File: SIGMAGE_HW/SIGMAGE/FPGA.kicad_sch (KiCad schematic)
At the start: 1 part, among them U8 LFE5U25F6BG256I

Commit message: some FPGA stuff
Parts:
- added C100, C101, C103, C104, C106, C107, C109, C110, C49, C51, C52, C53, C54, C55, C91, C92, C94, C95, C97, C98: 100n, Capacitor_SMD:C_0603_1608Metric, symbol Device:C
- added C102, C105, C108, C111, C50, C93, C96, C99: 10u, Capacitor_SMD:C_0603_1608Metric, symbol Device:C
- added R48, R49, R50, R51, R52, R53, R54, R55: 0, Resistor_SMD:R_0603_1608Metric, symbol Device:R
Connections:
- net GND: now also C100.2, C101.2, C102.2, C103.2, C104.2, C105.2, C106.2, C107.2, C108.2, C109.2, C110.2, C111.2, C49.2, C50.2, C51.2, C52.2, C53.2, C54.2, C55.2, C91.2, C92.2, C93.2, C94.2, C95.2, C96.2, C97.2, C98.2, C99.2
- net VCC_CORE: now also C49.1, C50.1, C51.1, C52.1, C53.1, C54.1, C55.1, R48.2
- net VCC_IO1: now reaches U8.F10 (VCCIO1_1)
- net VCC_IO1: now also U8.F11 (VCCIO1_2), C94.1, C95.1, C96.1, R50.2
- net VCC_IO0: now reaches U8.F6 (VCCIO0_1)
- net VCC_IO0: now also U8.F7 (VCCIO0_2), C91.1, C92.1, C93.1, R49.2
- net VCC_IO2: now reaches U8.H11 (VCCIO2_1)
- net VCC_IO2: now also U8.J11 (VCCIO2_2), C97.1, C98.1, C99.1, R51.2
- net VCC_IO7: now reaches U8.H6 (VCCIO7_1)
- net VCC_IO7: now also U8.H7 (VCCIO7_2), C106.1, C107.1, C108.1, R54.2
- net VCC_IO6: now reaches U8.J6 (VCCIO6_1)
- net VCC_IO6: now also U8.J7 (VCCIO6_2), C103.1, C104.1, C105.1, R53.2
- net VCC_IO3: now reaches U8.K11 (VCCIO3_1)
- net VCC_IO3: now also U8.L11 (VCCIO3_2), C100.1, C101.1, C102.1, R52.2
- net VCC_IO8: now reaches U8.L6 (VCCIO8)
- net VCC_IO8: now also C109.1, C110.1, C111.1, R55.2
- net FPGA_JTAG_TDO: now reaches U8.M10 (TDO)
- net FPGA_JTAG_TDI: now reaches U8.R11 (TDI)
- net FPGA_JTAG_TCK: now reaches U8.T10 (TCK)
- net FPGA_JTAG_TMS: now reaches U8.T11 (TMS)
- new net DVCC_1V2: R48.1
- new net DVCC_3V3: R49.1, R50.1, R51.1, R52.1, R53.1, R54.1, R55.1
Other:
- moved on the sheet: U8A, U8B, U8C, U8D, U8E, U8F, U8G, U8H, U8I

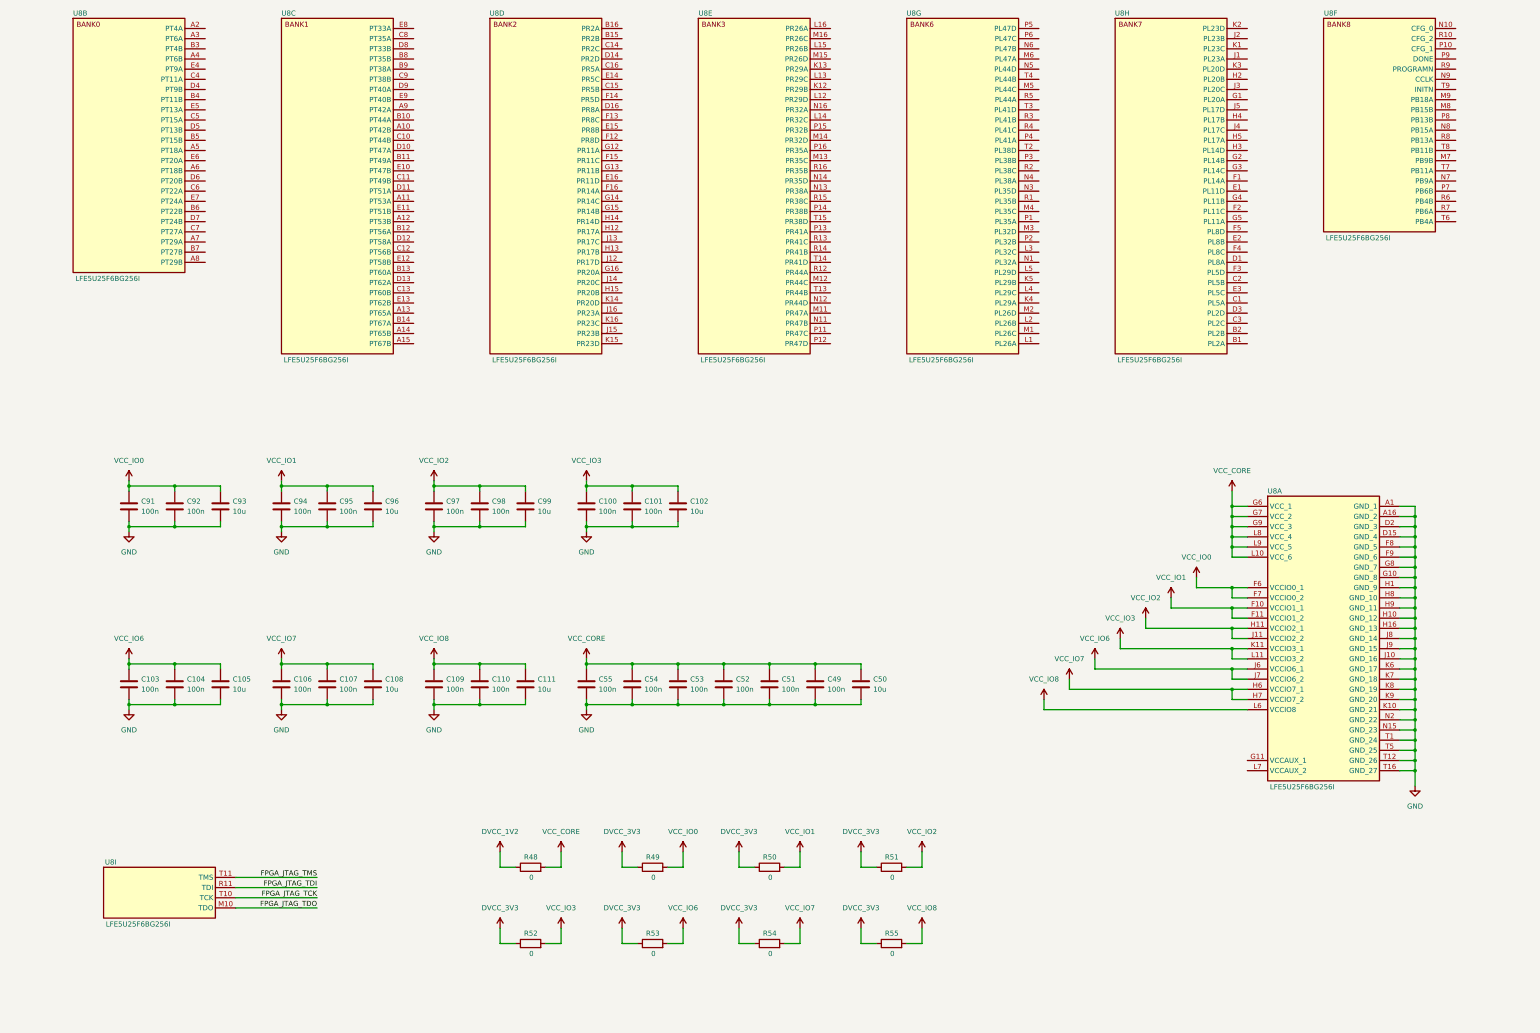
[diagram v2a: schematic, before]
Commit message: added SPI flash
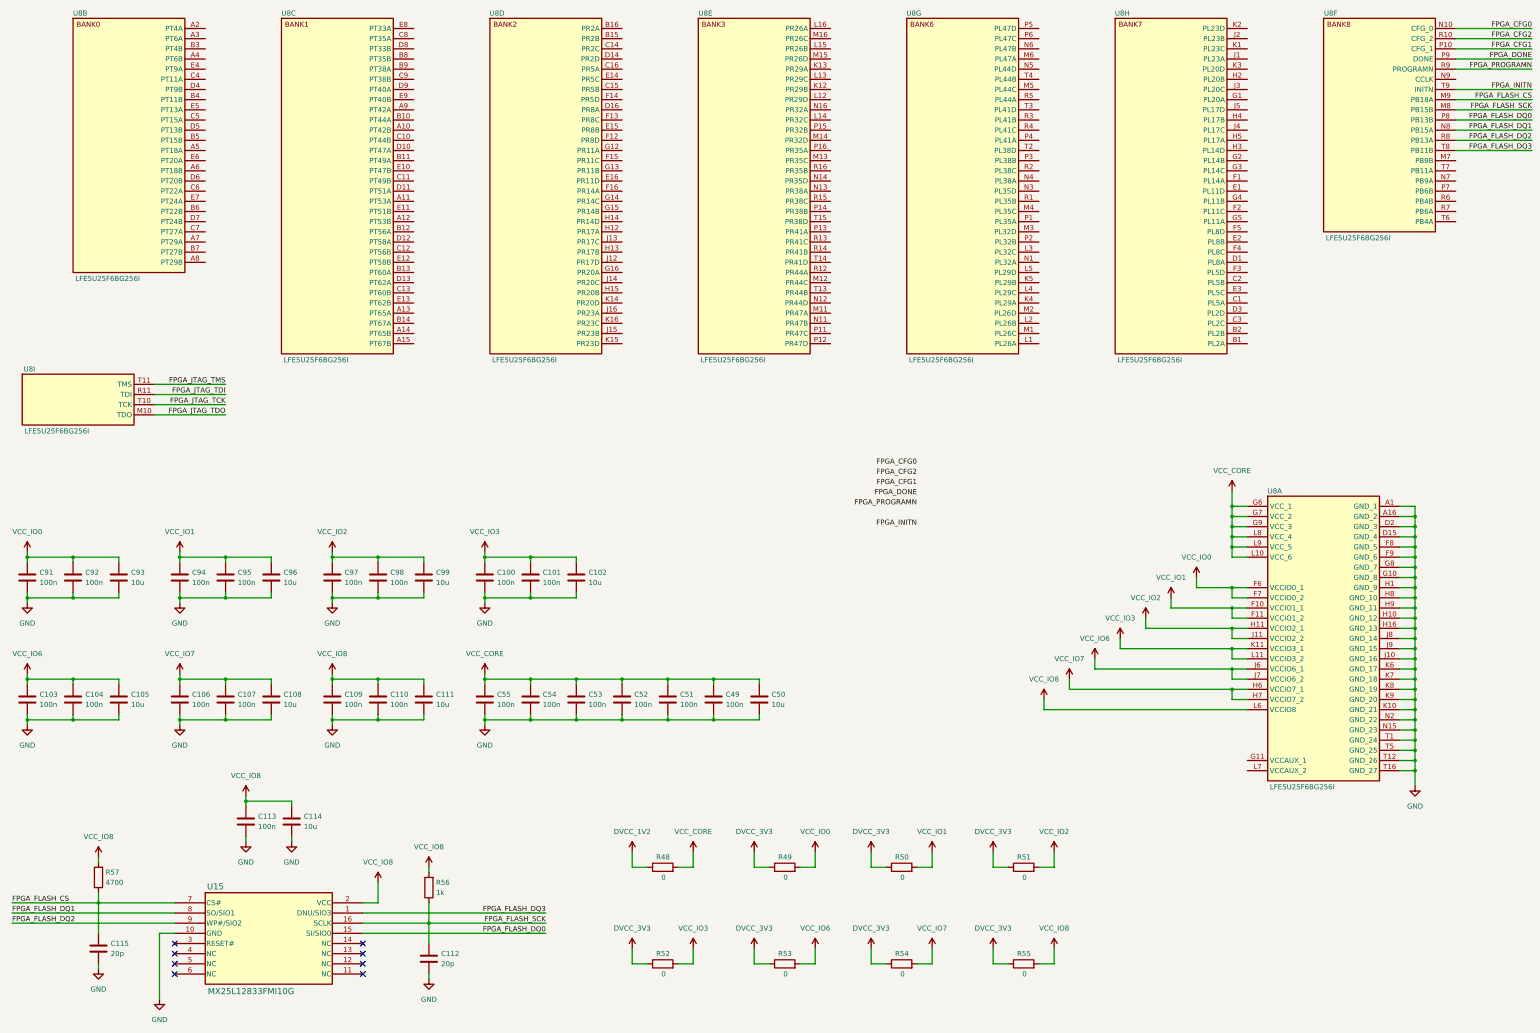
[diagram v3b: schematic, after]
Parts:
- added C112, C115: 20p, Capacitor_SMD:C_0603_1608Metric, symbol Device:C
- added C113: 100n, Capacitor_SMD:C_0603_1608Metric, symbol Device:C
- added C114: 10u, Capacitor_SMD:C_0603_1608Metric, symbol Device:C
- added R56: 1k, Resistor_SMD:R_0603_1608Metric, symbol Device:R
- added R57: 4700, Resistor_SMD:R_0603_1608Metric, symbol Device:R
- added U15: MX25L12833FMI10G, SIGMAGE:MX25L12833FMI10G, symbol SIGMAGE:MX25L12833FMI10G
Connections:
- net GND: now also C112.2, C113.2, C114.2, C115.2, U15.10 (GND)
- net VCC_IO8: now also C113.1, C114.1, R56.2, R57.2, U15.2 (VCC)
- net FPGA_FLASH_SCK: now reaches U8.M8 (PB15B)
- net FPGA_FLASH_SCK: now also C112.1, R56.1, U15.16 (SCLK)
- net FPGA_FLASH_CS: now reaches U8.M9 (PB18A)
- net FPGA_FLASH_CS: now also C115.1, R57.1, U15.7 (CS#)
- net FPGA_CFG0: now reaches U8.N10 (CFG_0)
- net FPGA_FLASH_DQ1: now reaches U8.N8 (PB15A)
- net FPGA_FLASH_DQ1: now also U15.8 (SO/SIO1)
- net FPGA_CFG1: now reaches U8.P10 (CFG_1)
- net FPGA_FLASH_DQ0: now reaches U8.P8 (PB13B)
- net FPGA_FLASH_DQ0: now also U15.15 (SI/SIO0)
- net FPGA_DONE: now reaches U8.P9 (DONE)
- net FPGA_CFG2: now reaches U8.R10 (CFG_2)
- net FPGA_FLASH_DQ2: now reaches U8.R8 (PB13A)
- net FPGA_FLASH_DQ2: now also U15.9 (WP#/SIO2)
- net FPGA_PROGRAMN: now reaches U8.R9 (PROGRAMN)
- net FPGA_FLASH_DQ3: now reaches U8.T8 (PB11B)
- net FPGA_FLASH_DQ3: now also U15.1 (DNU/SIO3)
- net FPGA_INITN: now reaches U8.T9 (INITN)
- no-connect marks 0 -> 8
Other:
- moved on the sheet: C100, C101, C102, C103, C104, C105, C106, C107, C108, C109, C110, C111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

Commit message: some changes
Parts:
- removed C112, C115: 20p, Capacitor_SMD:C_0603_1608Metric, symbol Device:C
- removed C113: 100n, Capacitor_SMD:C_0603_1608Metric, symbol Device:C
- removed C114: 10u, Capacitor_SMD:C_0603_1608Metric, symbol Device:C
- removed R56: 1k, Resistor_SMD:R_0603_1608Metric, symbol Device:R
- removed R57: 4700, Resistor_SMD:R_0603_1608Metric, symbol Device:R
- removed U15: MX25L12833FMI10G, SIGMAGE:MX25L12833FMI10G, symbol SIGMAGE:MX25L12833FMI10G
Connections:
- no-connect marks 8 -> 0

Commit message: changes
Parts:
- removed R48, R49, R50, R51, R52, R53, R54, R55: 0, Resistor_SMD:R_0603_1608Metric, symbol Device:R
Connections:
- net VCC_CORE is gone; now on net DVCC_1V2: C49.1, C50.1, C51.1, C52.1, C53.1, C54.1, C55.1, U8.G6 (VCC_1), U8.G7 (VCC_2), U8.G9 (VCC_3), U8.L10 (VCC_6), U8.L8 (VCC_4), U8.L9 (VCC_5)
- net VCC_IO0 is gone; now on net DVCC_3V3: C91.1, C92.1, C93.1, U8.F6 (VCCIO0_1), U8.F7 (VCCIO0_2)
- net VCC_IO1 is gone; now on net DVCC_3V3: C94.1, C95.1, C96.1, U8.F10 (VCCIO1_1), U8.F11 (VCCIO1_2)
- net VCC_IO2 is gone; now on net DVCC_3V3: C97.1, C98.1, C99.1, U8.H11 (VCCIO2_1), U8.J11 (VCCIO2_2)
- net VCC_IO3 is gone; now on net DVCC_3V3: C100.1, C101.1, C102.1, U8.K11 (VCCIO3_1), U8.L11 (VCCIO3_2)
- net VCC_IO6 is gone; now on net DVCC_3V3: C103.1, C104.1, C105.1, U8.J6 (VCCIO6_1), U8.J7 (VCCIO6_2)
- net VCC_IO7 is gone; now on net DVCC_3V3: C106.1, C107.1, C108.1, U8.H6 (VCCIO7_1), U8.H7 (VCCIO7_2)
- net VCC_IO8 is gone; now on net DVCC_3V3: C109.1, C110.1, C111.1, U8.L6 (VCCIO8)
- net FPGA_FLASH_CS: no longer names the net of U8.M9 (PB18A)
- net FPGA_FLASH_DQ0: no longer names the net of U8.P8 (PB13B)
- net FPGA_FLASH_DQ1: no longer names the net of U8.N8 (PB15A)
- net FPGA_FLASH_DQ2: no longer names the net of U8.R8 (PB13A)
- net FPGA_FLASH_DQ3: no longer names the net of U8.T8 (PB11B)
- net FPGA_FLASH_SCK: no longer names the net of U8.M8 (PB15B)

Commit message: major changes
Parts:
- added J9: TSW10607GS, SIGMAGE:TSW10607GS, symbol SIGMAGE:TSW10607GS
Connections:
- net GND: now also J9.6
- new net FPGA_USART1_RX: J9.2
- new net FPGA_USART1_TX: J9.1
- no-connect marks 0 -> 3
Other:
- moved on the sheet: U8B, U8C, U8D, U8E, U8F, U8G, U8H, U8I

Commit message: changes
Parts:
- added R110, R111, R112, R114, R115: 10k, Resistor_SMD:R_0603_1608Metric, symbol Device:R
- added R113: 1k, Resistor_SMD:R_0603_1608Metric, symbol Device:R
- added R116: 4700, Resistor_SMD:R_0603_1608Metric, symbol Device:R
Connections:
- net DVCC_3V3: now also R110.2, R111.2, R112.2, R113.2, R114.2, R115.2, R116.2
- net FPGA_DONE: now also R110.1
- net FPGA_INITN: now also R111.1
- net FPGA_PROGRAMN: now also R112.1
- net FPGA_USART1_RX: now also U8.T6 (PB4A)
- net FPGA_USART1_TX: now also U8.R7 (PB6A)
- net FPGA_SPI_CLK: now reaches U8.N9 (CCLK)
- net FPGA_SPI_CLK: now also R113.1
- net FPGA_SPI_CS: now reaches U8.R8 (PB13A)
- net FPGA_SPI_CS: now also R116.1
- net FPGA_SPI_MISO: now reaches U8.T7 (PB11A)
- net FPGA_SPI_MISO: now also R114.1
- net FPGA_SPI_MOSI: now reaches U8.T8 (PB11B)
- net FPGA_SPI_MOSI: now also R115.1
- no-connect marks 3 -> 10

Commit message: almost done
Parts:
- removed R112: 10k, Resistor_SMD:R_0603_1608Metric, symbol Device:R
- added C189: 1u, Capacitor_SMD:C_0603_1608Metric, symbol Device:C
- added C190, C191: 100n, Capacitor_SMD:C_0603_1608Metric, symbol Device:C
- added C192: 22u, Capacitor_SMD:C_0603_1608Metric, symbol Device:C
- added D261, D262: LED, LED_SMD:LED_0603_1608Metric, symbol Device:LED
- added FB10: 120 @ 100 MHz, Capacitor_SMD:C_0603_1608Metric, symbol Device:FerriteBead
- added R147, R148, R149, R151, R152, R153, R156: 10k, Resistor_SMD:R_0603_1608Metric, symbol Device:R
- added R150: 650, Resistor_SMD:R_0603_1608Metric, symbol Device:R
- added U41: MMBT2222A, SIGMAGE:MMBT2222A, symbol SIGMAGE:MMBT2222A
- R111: value 10k -> 650
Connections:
- net DVCC_3V3: now also R147.2, R148.2, R149.2, R150.2, R151.2, R152.2, R153.2, R156.2; no longer R110.2
- net FPGA_CFG0: now also R153.1
- net FPGA_CFG1: now also R152.1
- net FPGA_CFG2: now also R151.1
- net FPGA_DONE: now also R149.1
- net FPGA_INITN: now also D262.1 (K), R147.1; no longer R111.1
- net FPGA_PROGRAMN: now also R148.1
- net GND: now also C189.2, C190.2, C191.2, C192.2, U41.2
- net at U8.G11 (VCCAUX_1): now also U8.L7 (VCCAUX_2), C189.1, C190.1, C191.1, C192.1, FB10.2
- net FPGA_HOLDN: now reaches U8.N8 (PB15A)
- net FPGA_HOLDN: now also R156.1
- new net: D262.2 (A), R111.1
- new net: R110.2, U41.1
- new net: D261.1 (K), U41.3
- new net: D261.2 (A), R150.1
- new net DVCC_2V5: FB10.1
- no-connect marks 10 -> 3
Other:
- moved on the sheet: J9, U8A, U8I
